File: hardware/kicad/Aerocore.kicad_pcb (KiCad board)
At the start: 4 copper layers, 36 x 36 mm, 54 parts, among them J1 TYPE-C-31-M-12, J10 ESC3_PWM, J11 ESC4_PWR, J12 ESC4_PWM, J13 BAT_IN, J2 ELSR, J3 ST-LINK header, J4 5V_OUT, J5 ESC1_PWR, J6 ESC1_PWM, J7 ESC2_PWR, J8 ESC2_PWM, J9 ESC3_PWR, U1 STM32F411CEU6, U2 LMR51430, U3 TLV75533PDBV, U4 BMI270, Y1 16MHZ

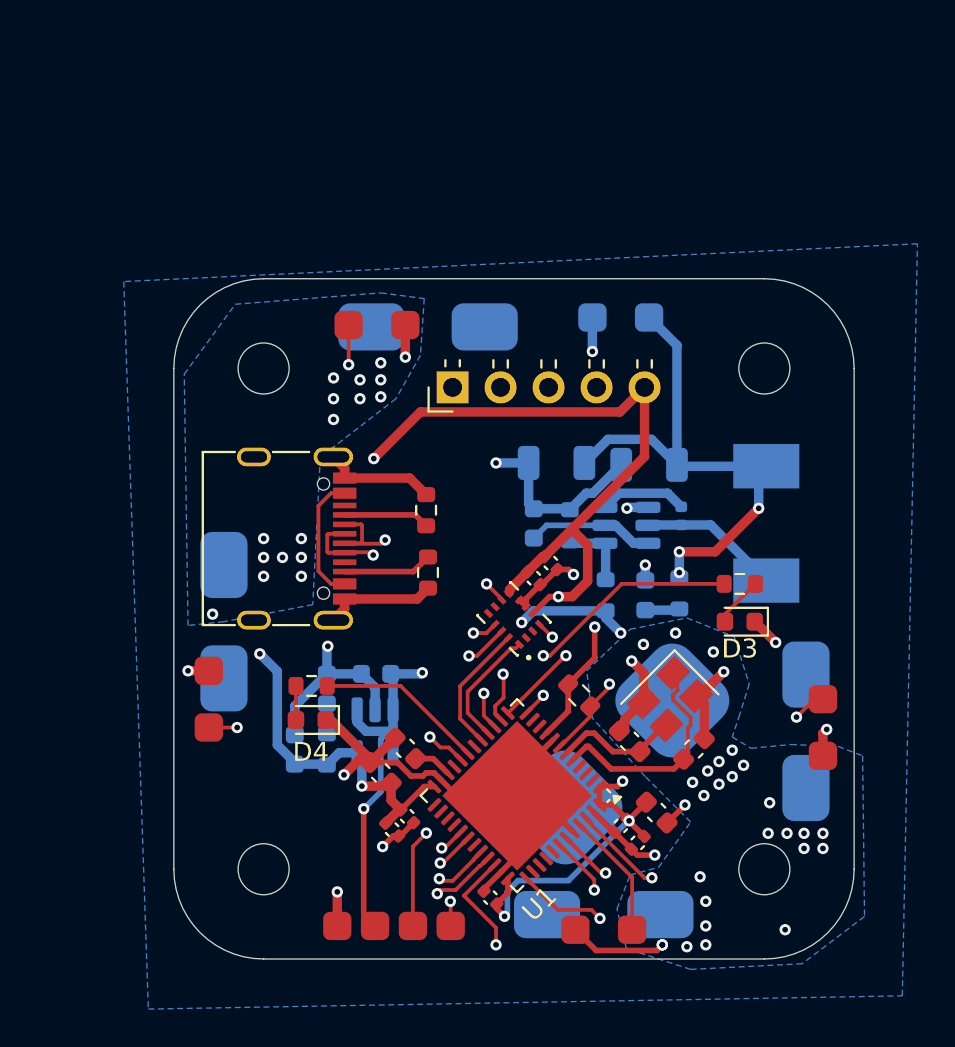
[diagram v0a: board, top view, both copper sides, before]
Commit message: Redesign PCB layout to fix power distribution issues
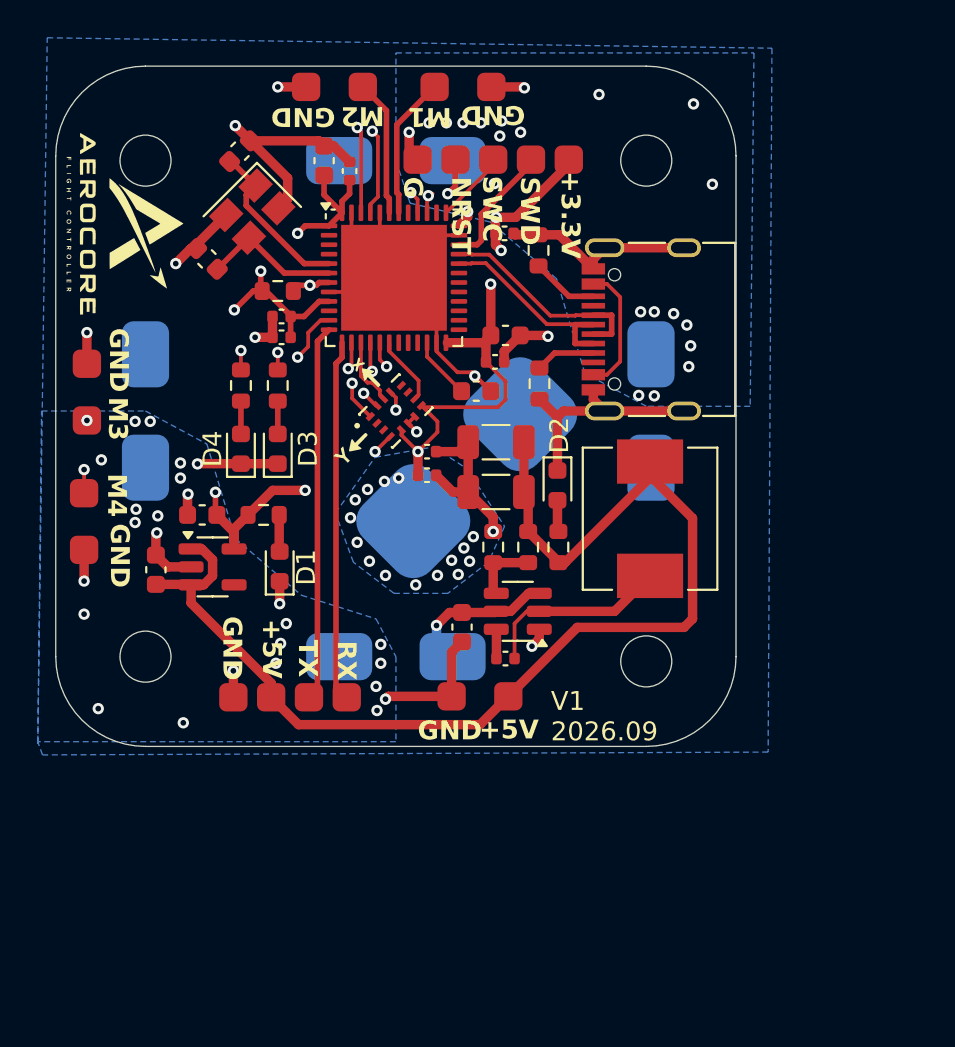
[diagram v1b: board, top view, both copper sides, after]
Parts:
- removed D5, D6: LED, LED_SMD:LED_0603_1608Metric
- removed R10, R11: 330, Resistor_SMD:R_0603_1608Metric
- added D1: LED, LED_SMD:LED_0603_1608Metric, F.Cu at (140.8, 90.5)
- added D2: LED, LED_SMD:LED_0603_1608Metric, F.Cu at (155.6, 86.2)
- added G***: LOGO, LOGO, F.Cu at (132.7, 72.3)
- added G***: LOGO, LOGO, F.Cu at (145.9, 80.7)
- added G***: LOGO, LOGO, F.Cu at (145.2, 83.7)
- added G***: LOGO, LOGO, B.Cu at (160.7, 90.1)
- added R2: 5K, Resistor_SMD:R_0603_1608Metric, F.Cu at (154.6, 73.8)
- added R7: 10k, Resistor_SMD:R_0603_1608Metric, F.Cu at (140.8, 75.9)
- C1: value 100n -> 10u; footprint Capacitor_SMD:C_0402_1005Metric -> Capacitor_SMD:C_0603_1608Metric
- C11: value 10u -> 100n; footprint Capacitor_SMD:C_0603_1608Metric -> Capacitor_SMD:C_0402_1005Metric; moved to F.Cu
- C12: value 100n -> 10p; footprint Capacitor_SMD:C_0402_1005Metric -> Capacitor_SMD:C_0603_1608Metric; moved to F.Cu
- C13, C14: value 22u -> 100n; footprint Capacitor_SMD:C_1206_3216Metric -> Capacitor_SMD:C_0402_1005Metric; moved to F.Cu
- C15: value 1u -> 4.7u; moved to F.Cu
- C16: value 1u -> 100n; footprint Capacitor_SMD:C_0603_1608Metric -> Capacitor_SMD:C_0402_1005Metric; moved to F.Cu
- C18, C3: value 100n -> 1u; footprint Capacitor_SMD:C_0402_1005Metric -> Capacitor_SMD:C_0603_1608Metric
- C5, C6: value 100n -> 22u; footprint Capacitor_SMD:C_0402_1005Metric -> Capacitor_SMD:C_1206_3216Metric
- C7, C8: value 4.7u -> 100n; footprint Capacitor_SMD:C_0603_1608Metric -> Capacitor_SMD:C_0402_1005Metric
- C9: value 10p -> 4.7u
- J1: value TYPE-C-31-M-12 -> 5V_OUT; footprint Connector_USB:USB_C_Receptacle_G-Switch_GT-USB-7010ASV -> Custom:Power_Pad_1.5x1.5mm
- J10: value ESC3_PWM -> ESC4_PWR; footprint Custom:Power_Pad_1.5x1.5mm -> Custom:Power_Pad_2.5x3.5mm; moved to B.Cu
- J11: value ESC4_PWR -> ESC4_PWM; footprint Custom:Power_Pad_2.5x3.5mm -> Custom:Power_Pad_1.5x1.5mm; moved to F.Cu
- J12: value ESC4_PWM -> ELSR; footprint Custom:Power_Pad_1.5x1.5mm -> Custom:Power_Pad_4_1.5x1.5mm
- J13: value BAT_IN -> ST-LINK header; footprint Custom:Power_Pad_4x5mm -> Custom:Solder_Pad_5_1.5x1.5mm; moved to F.Cu
- J2: value ELSR -> BAT_IN; footprint Custom:ELSR -> Custom:Power_Pad_4x5mm; moved to B.Cu
- J3: value ST-LINK header -> TYPE-C-31-M-12; footprint Connector_PinHeader_2.54mm:PinHeader_1x05_P2.54mm_Horizontal -> Connector_USB:USB_C_Receptacle_G-Switch_GT-USB-7010ASV
- J4: value 5V_OUT -> ESC1_PWR; footprint Custom:Power_Pad_1.5x1.5mm -> Custom:Power_Pad_2.5x3.5mm
- J5: value ESC1_PWR -> ESC1_PWM; footprint Custom:Power_Pad_2.5x3.5mm -> Custom:Power_Pad_1.5x1.5mm; moved to F.Cu
- J6: value ESC1_PWM -> ESC2_PWR; footprint Custom:Power_Pad_1.5x1.5mm -> Custom:Power_Pad_2.5x3.5mm; moved to B.Cu
- J7: value ESC2_PWR -> ESC2_PWM; footprint Custom:Power_Pad_2.5x3.5mm -> Custom:Power_Pad_1.5x1.5mm; moved to F.Cu
- J8: value ESC2_PWM -> ESC3_PWR; footprint Custom:Power_Pad_1.5x1.5mm -> Custom:Power_Pad_2.5x3.5mm; moved to B.Cu
- J9: value ESC3_PWR -> ESC3_PWM; footprint Custom:Power_Pad_2.5x3.5mm -> Custom:Power_Pad_1.5x1.5mm; moved to F.Cu
- L1, R3, R4: moved to F.Cu
- R1: value 10k -> 5K
- R5, R6: value 5K -> 330
- U1: value STM32F411CEU6 -> LMR51430; footprint Package_DFN_QFN:QFN-48-1EP_7x7mm_P0.5mm_EP5.6x5.6mm -> Package_TO_SOT_SMD:SOT-23-6
- U2: value LMR51430 -> TLV75533PDBV; footprint Package_TO_SOT_SMD:SOT-23-6 -> Package_TO_SOT_SMD:SOT-23-5; moved to F.Cu
- U3: value TLV75533PDBV -> BMI270; footprint Package_TO_SOT_SMD:SOT-23-5 -> Custom:XDCR_BMI270; moved to F.Cu
- U4: value BMI270 -> STM32F411CEU6; footprint MyFootprints:XDCR_BMI270 -> Package_DFN_QFN:QFN-48-1EP_7x7mm_P0.5mm_EP5.6x5.6mm
- moved J7 46.1 mm to (143.8, 65.1), turned to 180 degrees
- moved J11 39.8 mm to (130.5, 88.1)
- moved H1 38.0 mm to (160.2, 69.0)
- moved H2 38.0 mm to (133.8, 69.0)
- moved C10 37.4 mm to (138.8, 68.5), turned to 45 degrees
- moved C9 36.8 mm to (143.2, 69.0), turned to 90 degrees
- moved H3 36.1 mm to (133.8, 95.2)
- moved Y1 34.0 mm to (139.4, 71.7)
- moved J13 32.1 mm to (152.2, 69.0), turned to 0 degrees
- moved C2 29.5 mm to (134.3, 90.7), turned to 90 degrees
- moved C12 28.5 mm to (137.0, 74.2), turned to 135 degrees
- moved J12 28.2 mm to (141.4, 97.4), turned to 0 degrees
- moved C3 27.6 mm to (136.8, 87.8), turned to 180 degrees
- moved R8 26.6 mm to (140.8, 80.9), turned to 90 degrees
- moved D3 26.1 mm to (140.8, 84.2), turned to 90 degrees
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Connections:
- C1 pad 1: +3.3V -> +BATT
- C10 pad 1: /HSE_OUT -> /HSE_IN
- C11 pad 1: +BATT -> +3.3V
- C12 pad 1: Net-(U2-SW) -> /HSE_OUT
- C12 pad 2: Net-(U2-CB) -> GND
- C13 pad 1: +5V -> +3.3V
- C14 pad 1: +5V -> +3.3V
- C15 pad 1: +5V -> GND
- C15 pad 2: GND -> Net-(U4-VCAP1)
- C2 pad 1: +3.3V -> +5V
- C4 pad 1: +3.3V -> Net-(U1-SW)
- C4 pad 2: GND -> Net-(U1-CB)
- C5 pad 1: +3.3V -> +5V
- C6 pad 1: +3.3V -> +5V
- C8 pad 1: GND -> +3.3V
- C8 pad 2: Net-(U1-VCAP1) -> GND
- C9 pad 1: /HSE_IN -> +3.3V
- J11 pad 1: GND -> /TIM4_CH4
- J11 pad 2: +BATT -> GND
- J13 pad 1: +BATT -> GND
- J13 pad 2: GND -> /NRST
- J2 pad 1: GND -> +BATT
- J2 pad 2: +5V -> GND
- J4 pad 1: +5V -> GND
- J5 pad 1: GND -> /TIM4_CH1
- J5 pad 2: +BATT -> GND
- J7 pad 1: GND -> /TIM4_CH2
- J7 pad 2: +BATT -> GND
- J9 pad 1: GND -> /TIM4_CH3
- J9 pad 2: +BATT -> GND
- L1 pad 1: Net-(U2-SW) -> Net-(U1-SW)
- R1 pad 1: +3.3V -> Net-(J3-CC1)
- R1 pad 2: /NRST -> GND
- R3 pad 1: Net-(U2-FB) -> Net-(U1-FB)
- R4 pad 2: Net-(U2-FB) -> Net-(U1-FB)
- R5 pad 1: Net-(J1-CC1) -> +3.3V
- R5 pad 2: GND -> Net-(D1-A)
- R6 pad 1: GND -> +5V
- R6 pad 2: Net-(J1-CC2) -> Net-(D2-A)
- R8 pad 2: Net-(U1-PB2) -> Net-(U4-PB3)
- R9 pad 2: Net-(U1-PB1) -> Net-(U4-PB4)
- U1 pad 1: +3.3V -> GND
- U1 pad 2: unconnected-(U1-PC13-Pad2) -> Net-(U1-SW)
- U1 pad 3: unconnected-(U1-PC14-Pad3) -> +BATT
- U1 pad 4: unconnected-(U1-PC15-Pad4) -> Net-(U1-FB)
- U1 pad 5: /HSE_IN -> +BATT
- U1 pad 6: /HSE_OUT -> Net-(U1-CB)
- U2 pad 1: GND -> +5V
- U2 pad 2: Net-(U2-SW) -> GND
- U2 pad 3: +BATT -> +5V
- U2 pad 4: Net-(U2-FB) -> unconnected-(U2-NC-Pad4)
- U2 pad 5: +BATT -> +3.3V
- U3 pad 1: +5V -> /SPI1_MISO
- U3 pad 2: GND -> unconnected-(U3-ASDX-Pad2)
- U3 pad 3: +5V -> unconnected-(U3-ASCX-Pad3)
- U3 pad 4: unconnected-(U3-NC-Pad4) -> /IMU_INT1
- U4 pad 1: /SPI1_MISO -> +3.3V
- U4 pad 11: unconnected-(U4-OSDO-Pad11) -> /IMU_INT1
- U4 pad 12: /SPI1_CS -> /USART2_TX
- U4 pad 13: /SPI1_SCK -> /USART2_RX
- U4 pad 14: /SPI1_MOSI -> /SPI1_CS
- U4 pad 4: /IMU_INT1 -> unconnected-(U4-PC15-Pad4)
- U4 pad 5: +3.3V -> /HSE_IN
- U4 pad 6: GND -> /HSE_OUT
- U4 pad 7: GND -> /NRST
- U4 pad 8: +3.3V -> GND
- U4 pad 9: /IMU_INT2 -> +3.3V
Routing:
- net /SWIDO: track 51.5 -> 6.39 mm, vias 1 -> 0
- net /SWCLK: track 44.5 -> 3.85 mm, vias 1 -> 0
- net +3.3V: track 109.4 -> 75.1 mm, vias 8 -> 10
- net /TIM4_CH1: track 38.4 -> 7.53 mm, vias 2 -> 0
- net Net-(U1-PB2): track 21.1 -> 0.00 mm, vias 2 -> 0
- net /TIM4_CH3: track 6.69 -> 26.7 mm, vias 0 -> 2
- net /IMU_INT2: track 20.3 -> 3.69 mm, vias 2 -> 0
- net /USB_D+: track 27.3 -> 11.4 mm, vias 2 -> 0
- net /USB_D-: track 27.1 -> 11.4 mm, vias 2 -> 0
- net Net-(U4-PB4): track 0.00 -> 14.9 mm, vias 0 -> 2
- net Net-(U4-PB3): track 0.00 -> 13.7 mm, vias 0 -> 2
- net /TIM4_CH2: track 18.8 -> 7.24 mm, vias 2 -> 0
- net Net-(U1-SW): track 0.00 -> 10.1 mm
- net GND: track 97.3 -> 107.1 mm, vias 59 -> 71
- net Net-(U1-PB1): track 8.92 -> 0.00 mm
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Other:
- board text added: "+3.3V"
- board text added: "+5V"
- board text added: "+BATT"
- board text added: "G"
- board text added: "GND"
- board text added: "M1"
- board text added: "M2"
- board text added: "M3"
- board text added: "M4"
- board text added: "NRST"
- board text added: "RX"
- board text added: "SWC"
- board text added: "SWD"
- board text added: "TX"
- board text added: "V1 2026.09"
- board text added: "VBAT"
